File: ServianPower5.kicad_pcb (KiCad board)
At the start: 2 copper layers, 15 parts, among them J1 USB_C_Receptacle_USB2.0, J2 114020164, U1 TPS63002, U2 FT201XQ

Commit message: Updated with component details
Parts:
- R1: value 100Ohm -> 100 Ohm
- R4, R5: value 1000 -> 1k Ohms
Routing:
- net GND: track 15.1 -> 24.6 mm, vias 4 -> 6

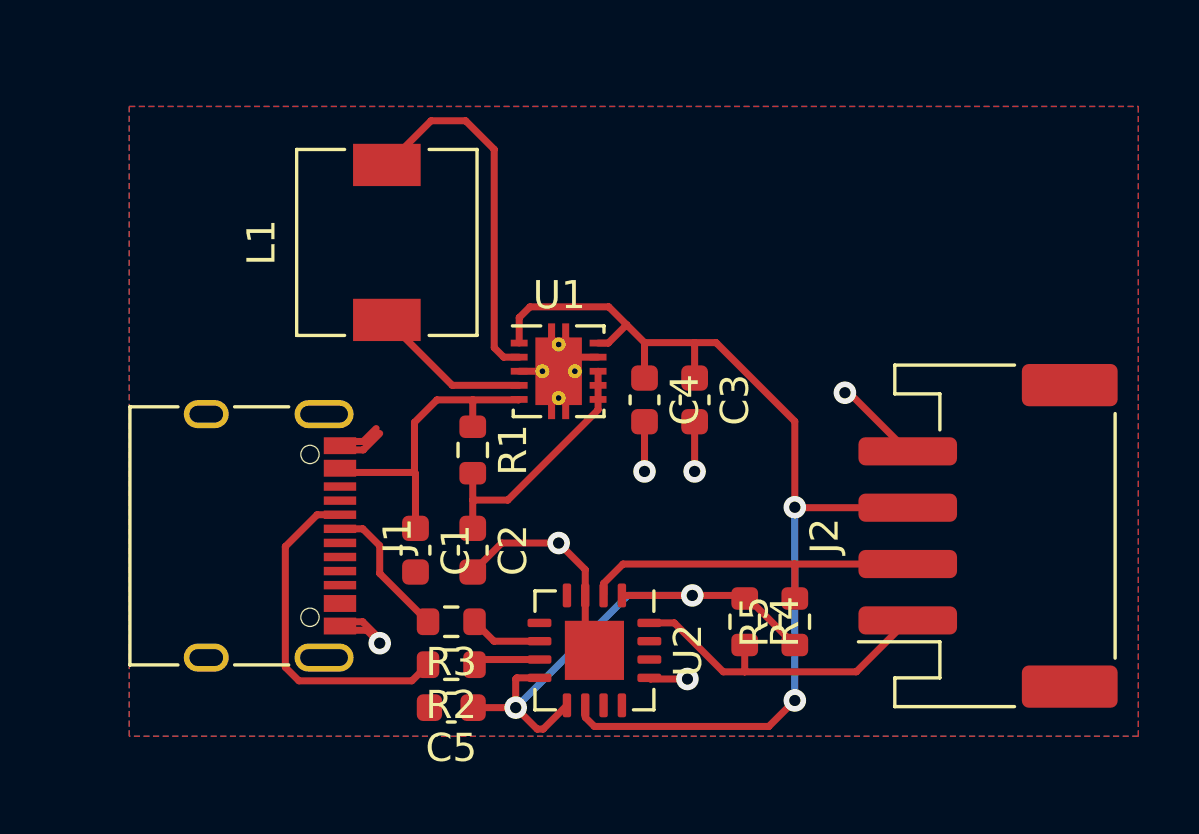
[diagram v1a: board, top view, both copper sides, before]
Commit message: Updated with component details for JLPCB
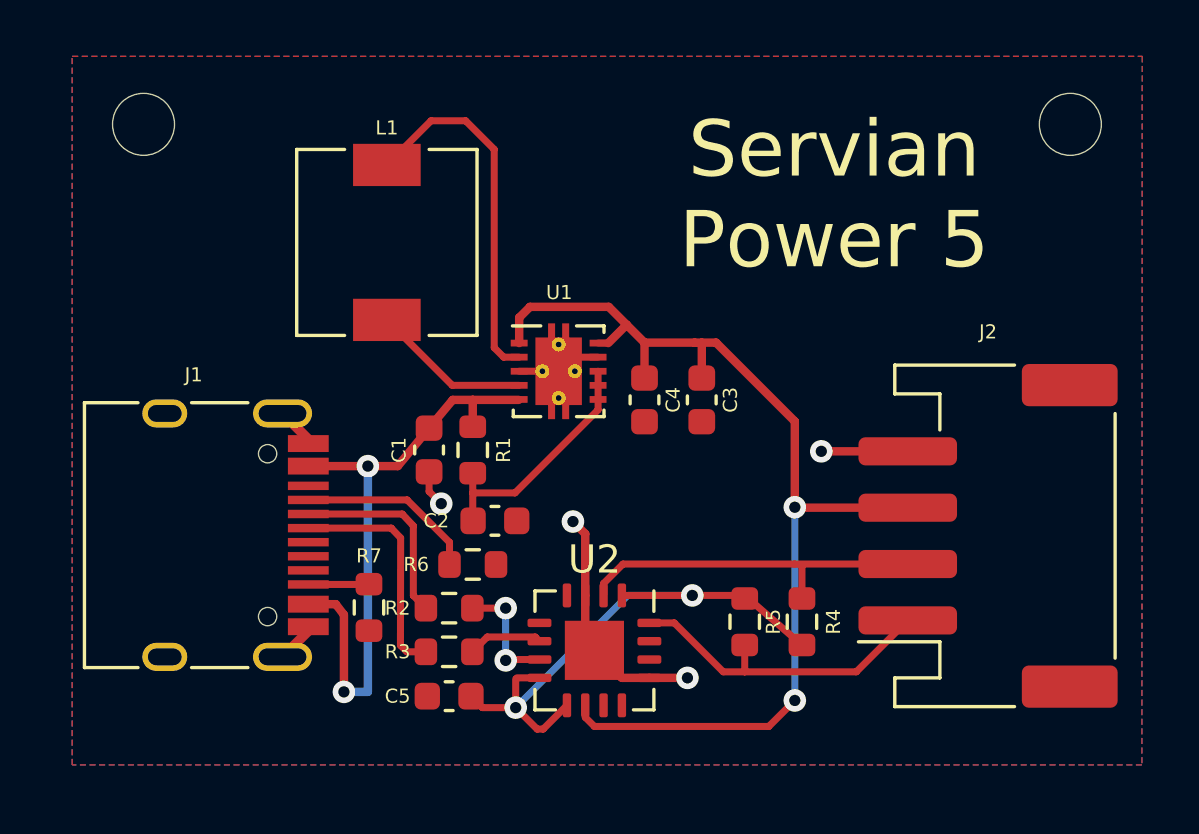
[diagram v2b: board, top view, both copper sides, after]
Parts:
- added MOUNT_TL: Mount_Top_Left, MountingHole:MountingHole_2.2mm_M2_ISO7380, F.Cu at (127.5, 74.3)
- added R6: 5.1k Ohm, Resistor_SMD:R_0603_1608Metric, F.Cu at (139.2, 89.9)
- added R7: 5.1k Ohm, Resistor_SMD:R_0603_1608Metric, F.Cu at (135.5, 91.4)
- added REF**: Mount_Top_Right, MountingHole:MountingHole_2.2mm_M2_ISO7380, F.Cu at (160.4, 74.3)
- C1, C3, C4: value 10uf -> 10uF
- C2: value 0.1uf -> 0.1uF
- C5: value 100nF -> 0.1uF
- J1: value USB_C_Receptacle_USB2.0 -> USB_C_Receptacle; footprint Connector_USB:USB_C_Receptacle_XKB_U262-16XN-4BVC11 -> Connector_USB:USB_C_Receptacle_HRO_TYPE-C-31-M-12
- R4, R5: value 1k Ohms -> 1k Ohm
- moved C1 3.59 mm to (137.6, 85.9)
- moved R2 2.01 mm to (138.4, 91.5)
- moved J1 1.50 mm to (129.3, 88.9)
- moved C2 1.31 mm to (140.0, 88.4), turned to 0 degrees
- moved R3 1.07 mm to (138.4, 93.0)
- moved C5 0.41 mm to (138.4, 94.6)
- moved C3 0.25 mm to (147.3, 84.1)
- moved R5 0.25 mm to (150.9, 91.9)
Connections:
- J1 pad S1: Net-(J1-PadS1) -> GND
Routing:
- net VBUS: track 11.7 -> 22.6 mm, vias 0 -> 2
- net Net-(J1-PadA5): track 0.00 -> 6.42 mm
- net GND: track 24.6 -> 18.3 mm, vias 6 -> 4
- net /USBDM: track 12.2 -> 7.01 mm
- net /USBDP: track 5.07 -> 8.24 mm
- net Net-(J1-PadB5): track 0.00 -> 2.18 mm
- net Net-(R2-Pad1): track 2.38 -> 4.28 mm, vias 0 -> 2
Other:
- board text added: "+5v"
- board text added: "GND"
- board text added: "Revision 0.1"
- board text added: "SCL"
- board text added: "SDA"
- board text added: "Servian Power 5"

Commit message: Updated footprint for L1
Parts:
- J1: value USB_C_Receptacle -> USB_C_Receptacle_USB2.0
- L1: footprint Inductor_SMD:L_6.3x6.3_H3 -> Inductor_SMD:L_TDK_VLS4012
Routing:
- net Net-(L1-Pad2): track 12.9 -> 9.12 mm
- net Net-(L1-Pad1): track 5.66 -> 6.22 mm
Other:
- board outline added: 37 x 24.4 mm
- board text added: "Grove Power 5"
- board text added: "by Timothy Findlay 2021"
- board text removed: "Servian Power 5"
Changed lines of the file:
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@@
   (general
     (thickness 1.6)
-    (drawings 7)
-    (tracks 130)
+    (drawings 16)
+    (tracks 129)
     (zones 0)
     (modules 19)
@@
     (34 B.Paste user)
     (35 F.Paste user)
-    (36 B.SilkS user hide)
-    (37 F.SilkS user hide)
+    (36 B.SilkS user)
+    (37 F.SilkS user)
     (38 B.Mask user)
     (39 F.Mask user)
@@
       (plotinvisibletext false)
       (padsonsilk false)
-      (subtractmaskfromsilk true)
+      (subtractmaskfromsilk false)
       (outputformat 1)
       (mirror false)
       (drillshape 0)
       (scaleselection 1)
-      (outputdirectory "Gerber20210929/"))
+      (outputdirectory "Gerber20211026/"))
   )
   (net 0 "")
@@
     (add_net VBUS)
   )
+  (module Inductor_SMD:L_TDK_VLS4012 (layer F.Cu)
+    (at 136.144 78.486 90)
+    (fp_text reference L1 (at 0 0 90) (layer F.SilkS)
+      (effects (font (size 1 1) (thickness 0.15)))
+    )
+    (fp_text value 2.2uH (at 0 -3.048 90) (layer F.Fab)
+      (effects (font (size 1 1) (thickness 0.15)))
+    )
+    (fp_line (start -2.1 2.1) (end -2.1 -2.1) (layer F.SilkS) (width 0.12))
+    (fp_line (start 2.1 2.1) (end -2.1 2.1) (layer F.SilkS) (width 0.12))
+    (fp_line (start 2.1 -2.1) (end 2.1 2.1) (layer F.SilkS) (width 0.12))
+    (fp_line (start -2.1 -2.1) (end 2.1 -2.1) (layer F.SilkS) (width 0.12))
+    (fp_line (start 2.2 2.3) (end 2.2 -2.3) (layer F.CrtYd) (width 0.12))
+    (fp_line (start -2.2 2.3) (end 2.2 2.3) (layer F.CrtYd) (width 0.12))
+    (fp_line (start -2.2 2.3) (end -2.2 -2.3) (layer F.CrtYd) (width 0.12))
+    (fp_line (start -2.2 -2.3) (end 2.2 -2.3) (layer F.CrtYd) (width 0.12))
+    (pad 2 smd rect (at 1.4 0 90) (size 1.3 4.4) (layers F.Cu F.Paste F.Mask)
+      (net 9 "Net-(L1-Pad2)"))
+    (pad 1 smd rect (at -1.4 0 90) (size 1.3 4.4) (layers F.Cu F.Paste F.Mask)
+      (net 10 "Net-(L1-Pad1)"))
+    (model ${KISYS3DMOD}/Inductor_SMD.3dshapes/L_TDK_VLS4012.step
+      (at (xyz 0 0 0))
+      (scale (xyz 1 1 1))
+      (rotate (xyz -90 0 0))
+    )
+  )
   (module MountingHole:MountingHole_2.2mm_M2_ISO7380 (layer F.Cu)
     (at 127.508 74.295)
@@
       (effects (font (size 0.5 0.5) (thickness 0.1)))
     )
-    (fp_text value USB_C_Receptacle (at 0 3.0734 90) (layer F.Fab)
+    (fp_text value USB_C_Receptacle_USB2.0 (at 0 3.0734 90) (layer F.Fab)
       (effects (font (size 0.5 0.5) (thickness 0.1)))
     )
@@
     (pad S1 thru_hole oval (at 4.32 1.05 270) (size 1 1.6) (drill oval 0.6 1.2) (layers *.Cu *.Mask)
       (net 1 GND))
-    (model ${KISYS3DMOD}/Connector_USB.3dshapes/USB_C_Receptacle_HRO_TYPE-C-31-M-12.wrl
-      (at (xyz 0 0 0))
-      (scale (xyz 1 1 1))
-      (rotate (xyz 0 0 0))
+    (model ${KISYS3DMOD}/Connector_USB.3dshapes/u262-241n-4bv64.step
+      (offset (xyz 0 -3.4 1.778))
+      (scale (xyz 1 1 1))
+      (rotate (xyz 90 180 180))
     )
   )
@@
     (pad MP smd roundrect (at -5.35 2.9 90) (size 1.5 3.4) (layers F.Cu F.Paste F.Mask) (roundrect_rratio 0.1666666666666667))
     (pad MP smd roundrect (at 5.35 2.9 90) (size 1.5 3.4) (layers F.Cu F.Paste F.Mask) (roundrect_rratio 0.1666666666666667))
-    (model ${KISYS3DMOD}/Connector_JST.3dshapes/JST_PH_S4B-PH-SM4-TB_1x04-1MP_P2.00mm_Horizontal.wrl
-      (at (xyz 0 0 0))
+    (model ${KISYS3DMOD}/Connector_JST.3dshapes/JST_PH_S4B-PH-K_1x04_P2.00mm_Horizontal.step
+      (offset (xyz -3 1.5 0))
       (scale (xyz 1 1 1))
       (rotate (xyz 0 0 0))
@@
     (pad "" smd roundrect (at 0 0.63) (size 1.5 1.06) (layers F.Paste) (roundrect_rratio 0.1)
       (zone_connect 0))
-    (model ${KISYS3DMOD}/Package_SON.3dshapes/Texas_DRC0010J.wrl
+    (model ${KISYS3DMOD}/Package_SON.3dshapes/VSON-10-1EP_3x3mm_P0.5mm_EP1.65x2.4mm.wrl
       (at (xyz 0 0 0))
       (scale (xyz 1 1 1))
@@
     )
   )
-  (module Inductor_SMD:L_6.3x6.3_H3 (layer F.Cu)
-    (at 136.144 78.486 90)
-    (descr "Choke, SMD, 6.3x6.3mm 3mm height")
-    (tags "Choke SMD")
-    (attr smd)
-    (fp_text reference L1 (at 4.064 0 180) (layer F.SilkS)
-      (effects (font (size 0.5 0.5) (thickness 0.1)))
-    )
-    (fp_text value 2.2uH (at -0.762 0 180) (layer F.Fab)
-      (effects (font (size 1 1) (thickness 0.15)))
-    )
-    (fp_line (start -3.15 3.15) (end 3.15 3.15) (layer F.Fab) (width 0.1))
-    (fp_line (start -3.15 -3.15) (end 3.15 -3.15) (layer F.Fab) (width 0.1))
-    (fp_line (start -3.15 -3.15) (end -3.15 -1.5) (layer F.Fab) (width 0.1))
-    (fp_line (start -3.15 3.15) (end -3.15 1.5) (layer F.Fab) (width 0.1))
-    (fp_line (start 3.15 -3.15) (end 3.15 -1.5) (layer F.Fab) (width 0.1))
-    (fp_line (start 3.15 3.15) (end 3.15 1.5) (layer F.Fab) (width 0.1))
-    (fp_line (start 3.75 -3.4) (end -3.75 -3.4) (layer F.CrtYd) (width 0.05))
-    (fp_line (start 3.75 3.4) (end 3.75 -3.4) (layer F.CrtYd) (width 0.05))
-    (fp_line (start -3.75 3.4) (end 3.75 3.4) (layer F.CrtYd) (width 0.05))
-    (fp_line (start -3.75 -3.4) (end -3.75 3.4) (layer F.CrtYd) (width 0.05))
-    (fp_line (start 3.3 -3.2) (end 3.3 -1.5) (layer F.SilkS) (width 0.12))
-    (fp_line (start -3.3 -3.2) (end 3.3 -3.2) (layer F.SilkS) (width 0.12))
-    (fp_line (start -3.3 -1.5) (end -3.3 -3.2) (layer F.SilkS) (width 0.12))
-    (fp_line (start -3.3 3.2) (end -3.3 1.5) (layer F.SilkS) (width 0.12))
-    (fp_line (start 3.3 3.2) (end -3.3 3.2) (layer F.SilkS) (width 0.12))
-    (fp_line (start 3.3 1.5) (end 3.3 3.2) (layer F.SilkS) (width 0.12))
-    (fp_arc (start 0 0) (end 1.91 1.91) (angle 90) (layer F.Fab) (width 0.1))
-    (fp_arc (start 0 0) (end -1.91 -1.91) (angle 90) (layer F.Fab) (width 0.1))
-    (fp_text user %R (at 0.762 0 180) (layer F.Fab)
-      (effects (font (size 1 1) (thickness 0.15)))
-    )
-    (pad 2 smd rect (at 2.75 0 90) (size 1.5 2.4) (layers F.Cu F.Paste F.Mask)
-      (net 9 "Net-(L1-Pad2)"))
-    (pad 1 smd rect (at -2.75 0 90) (size 1.5 2.4) (layers F.Cu F.Paste F.Mask)
-      (net 10 "Net-(L1-Pad1)"))
-    (model ${KISYS3DMOD}/Inductor_SMD.3dshapes/L_6.3x6.3_H3.wrl
-      (at (xyz 0 0 0))
-      (scale (xyz 1 1 1))
-      (rotate (xyz 0 0 0))
-    )
-  )
   (module Capacitor_SMD:C_0603_1608Metric (layer F.Cu)
     (at 138.3538 94.5896 180)
@@
     )
   )
+  (gr_arc (start 125.73 72.517) (end 125.73 72.263) (angle -90) (layer Edge.Cuts) (width 0.05))
+  (gr_arc (start 125.73 96.393) (end 125.476 96.393) (angle -90) (layer Edge.Cuts) (width 0.05))
+  (gr_arc (start 162.179 96.393) (end 162.179 96.647) (angle -90) (layer Edge.Cuts) (width 0.05))
+  (gr_arc (start 162.179 72.517) (end 162.433 72.517) (angle -90) (layer Edge.Cuts) (width 0.05))
+  (gr_line (start 125.73 72.263) (end 162.179 72.263) (layer Edge.Cuts) (width 0.05))
+  (gr_line (start 125.476 96.393) (end 125.476 72.517) (layer Edge.Cuts) (width 0.05))
+  (gr_line (start 162.179 96.647) (end 125.73 96.647) (layer Edge.Cuts) (width 0.05))
+  (gr_line (start 162.433 72.517) (end 162.433 96.393) (layer Edge.Cuts) (width 0.05))
+  (gr_text "by Timothy Findlay 2021" (at 144.526 74.295) (layer B.SilkS)
+    (effects (font (size 1 1) (thickness 0.15)) (justify mirror))
+  )
   (gr_text "Revision 0.1" (at 132.08 95.758) (layer B.SilkS)
     (effects (font (size 1 1) (thickness 0.15)) (justify mirror))
@@
   )
   (gr_poly (pts (xy 162.9156 97.0026) (xy 124.9934 97.0026) (xy 124.9934 71.9074) (xy 162.9156 71.9074)) (layer Margin) (width 0.1))
-  (gr_text "Servian\nPower 5" (at 152.019 76.7969) (layer F.SilkS)
+  (gr_text "Grove\nPower 5" (at 152.019 76.7969) (layer F.SilkS)
     (effects (font (size 2 2) (thickness 0.15)))
   )
@@
   (segment (start 135.4994 90.6246) (end 135.509 90.615) (width 0.25) (layer F.Cu) (net 8))
   (segment (start 133.3564 90.6246) (end 135.4994 90.6246) (width 0.25) (layer F.Cu) (net 8))
-  (segment (start 140.29 82.558) (end 139.954 82.222) (width 0.25) (layer F.Cu) (net 9))
-  (segment (start 140.84 82.558) (end 140.29 82.558) (width 0.25) (layer F.Cu) (net 9))
-  (segment (start 139.954 82.222) (end 139.954 75.184) (width 0.25) (layer F.Cu) (net 9))
-  (segment (start 139.954 75.184) (end 138.938 74.168) (width 0.25) (layer F.Cu) (net 9))
-  (segment (start 137.712 74.168) (end 136.144 75.736) (width 0.25) (layer F.Cu) (net 9))
-  (segment (start 138.938 74.168) (end 137.712 74.168) (width 0.25) (layer F.Cu) (net 9))
-  (segment (start 138.466 83.558) (end 136.144 81.236) (width 0.25) (layer F.Cu) (net 10))
-  (segment (start 140.84 83.558) (end 138.466 83.558) (width 0.25) (layer F.Cu) (net 10))
+  (segment (start 140.84 82.558) (end 140.29 82.558) (width 0.3) (layer F.Cu) (net 9))
+  (segment (start 138.594 77.086) (end 136.144 77.086) (width 0.3) (layer F.Cu) (net 9))
+  (segment (start 138.938 77.47) (end 138.594 77.086) (width 0.3) (layer F.Cu) (net 9))
+  (segment (start 138.938 81.28) (end 138.938 77.47) (width 0.3) (layer F.Cu) (net 9))
+  (segment (start 140.208 82.55) (end 138.938 81.28) (width 0.3) (layer F.Cu) (net 9))
+  (segment (start 139.816 83.558) (end 136.144 79.886) (width 0.3) (layer F.Cu) (net 10))
+  (segment (start 140.84 83.558) (end 139.816 83.558) (width 0.3) (layer F.Cu) (net 10))
   (via (at 140.3604 91.4654) (size 0.8) (drill 0.4) (layers F.Cu B.Cu) (net 11))
   (via (at 140.3604 93.3196) (size 0.8) (drill 0.4) (layers F.Cu B.Cu) (net 11))

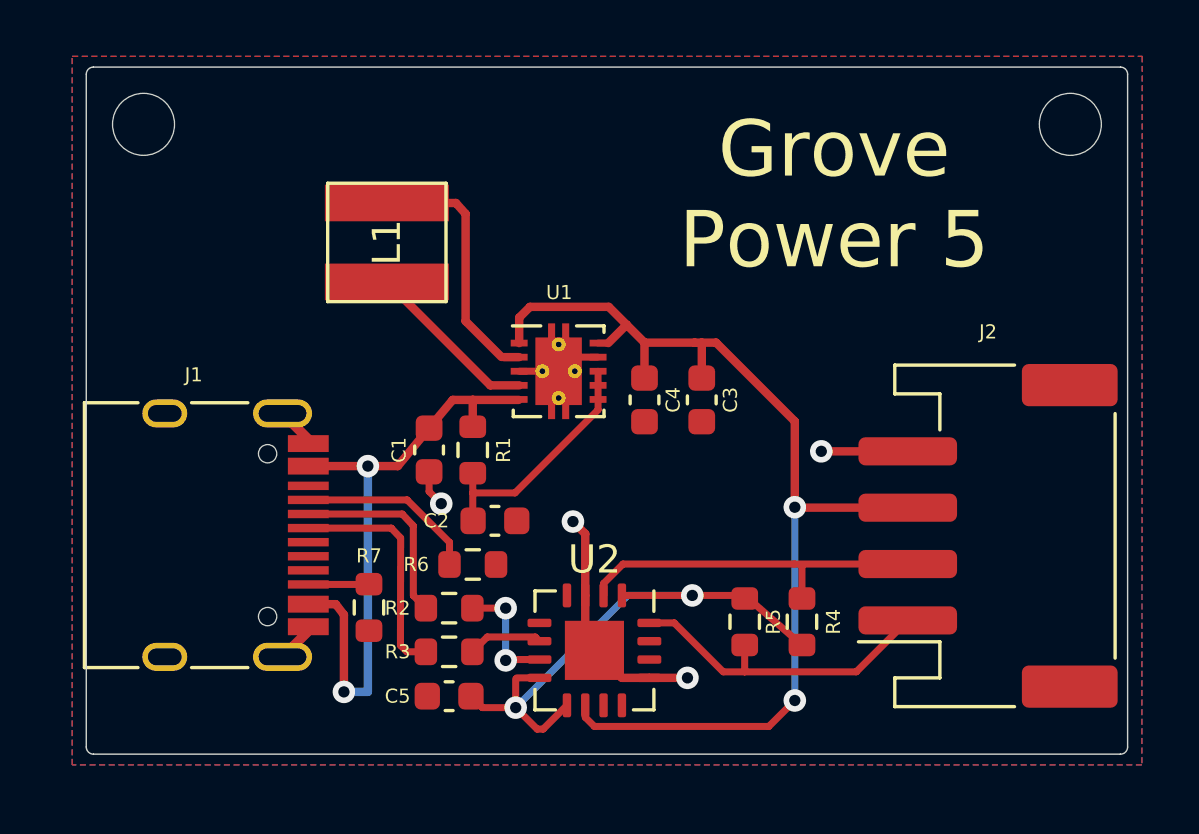
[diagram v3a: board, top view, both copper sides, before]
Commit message: Added images, updated README and reduced the board size
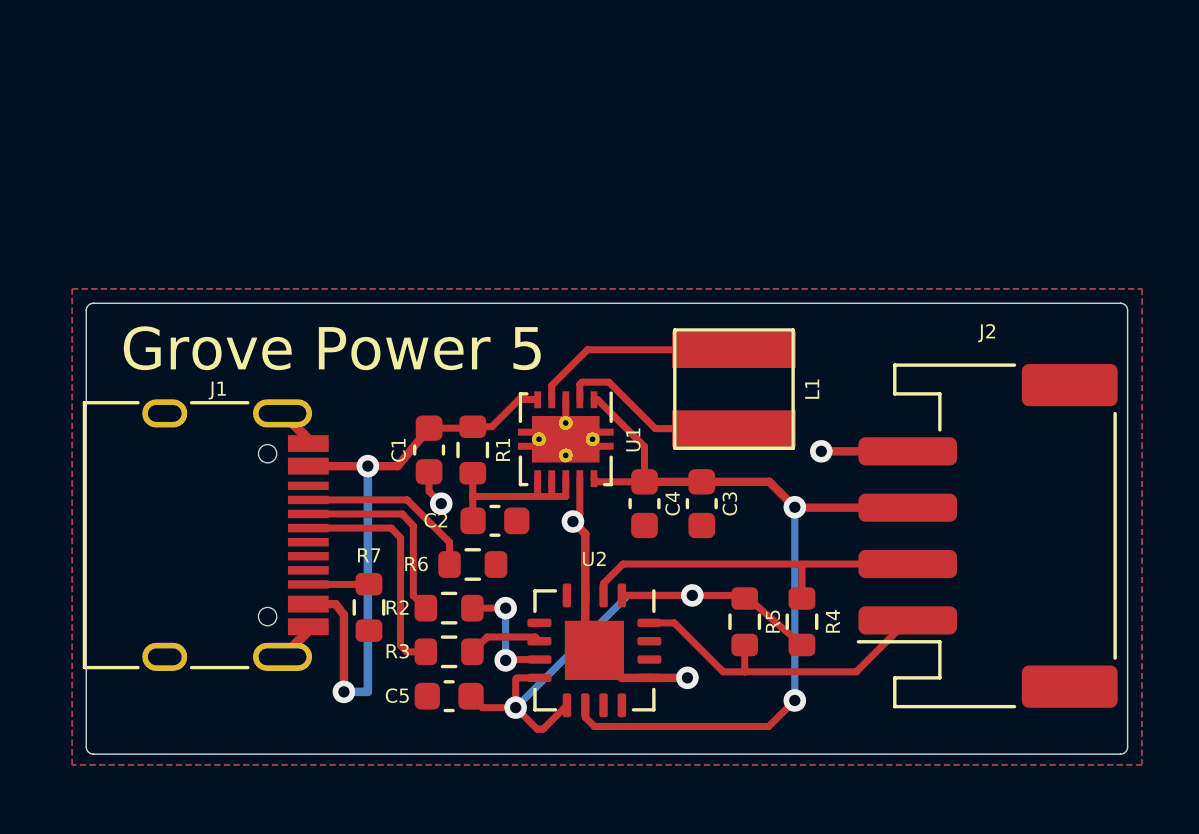
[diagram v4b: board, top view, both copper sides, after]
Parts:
- removed MOUNT_TL: Mount_Top_Left, MountingHole:MountingHole_2.2mm_M2_ISO7380
- removed REF**: Mount_Top_Right, MountingHole:MountingHole_2.2mm_M2_ISO7380
- moved L1 13.4 mm to (148.5, 83.7), turned to 270 degrees
- moved C3 3.68 mm to (147.3, 87.8)
- moved C4 3.68 mm to (145.3, 87.8)
- moved U1 2.43 mm to (142.5, 85.5), turned to 270 degrees
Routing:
- net +5V: track 38.6 -> 30.5 mm
- net Net-(L1-Pad2): track 9.12 -> 6.73 mm
- net Net-(C2-Pad1): track 8.75 -> 6.92 mm
- net Net-(L1-Pad1): track 6.22 -> 7.50 mm
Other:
- board size 37 x 24.4 mm -> 37 x 16 mm
- board text added: "Revision 0.2"
- board text removed: "Revision 0.1"
